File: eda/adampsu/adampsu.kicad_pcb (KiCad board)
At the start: 2 copper layers, 78.7 x 60.8 mm, 57 parts, among them J1 Barrel_Jack_Switch, J2 Conn_2Rows-09Pins, J3 DB9_Female, Q1 BUK7880-55A_CUX, SW1 30V 300mA Latching Switch, U1 TPS561201, U2 TPS54531DDAR

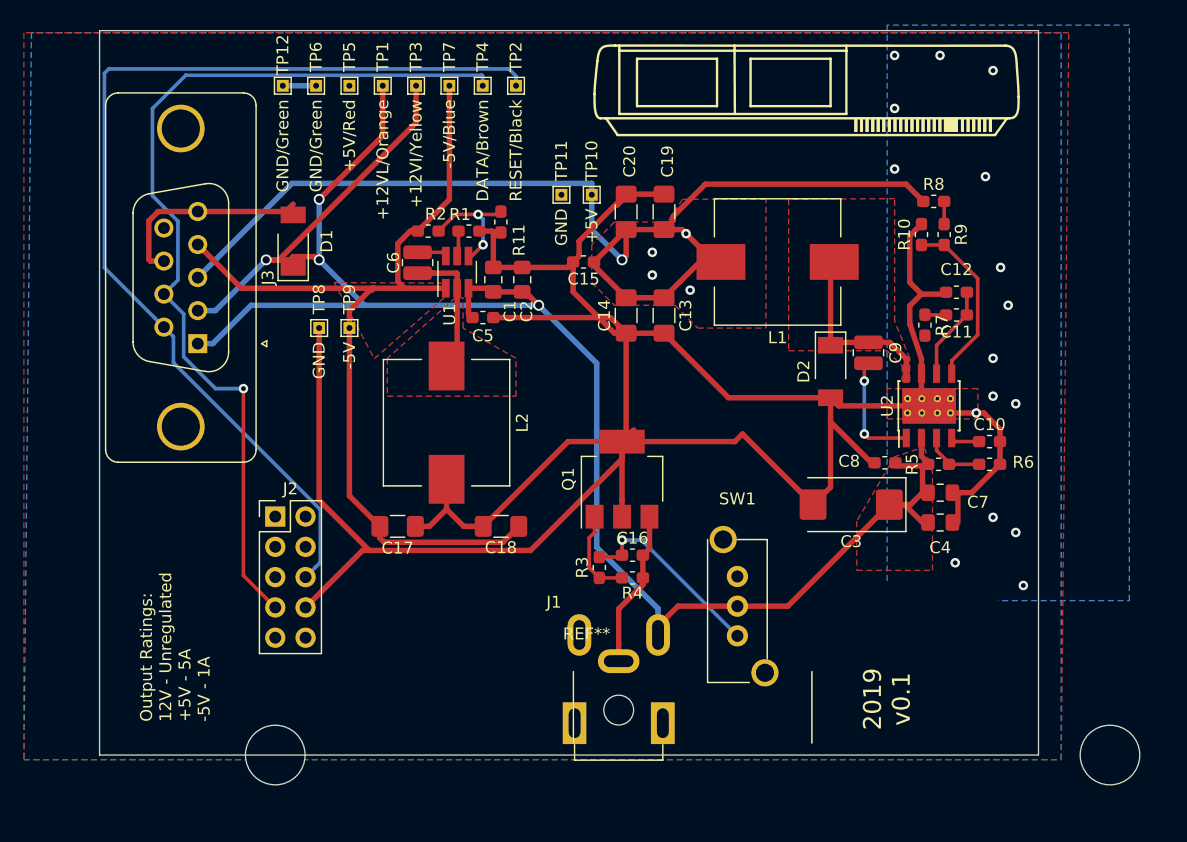
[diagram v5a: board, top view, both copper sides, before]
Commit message: high side switching
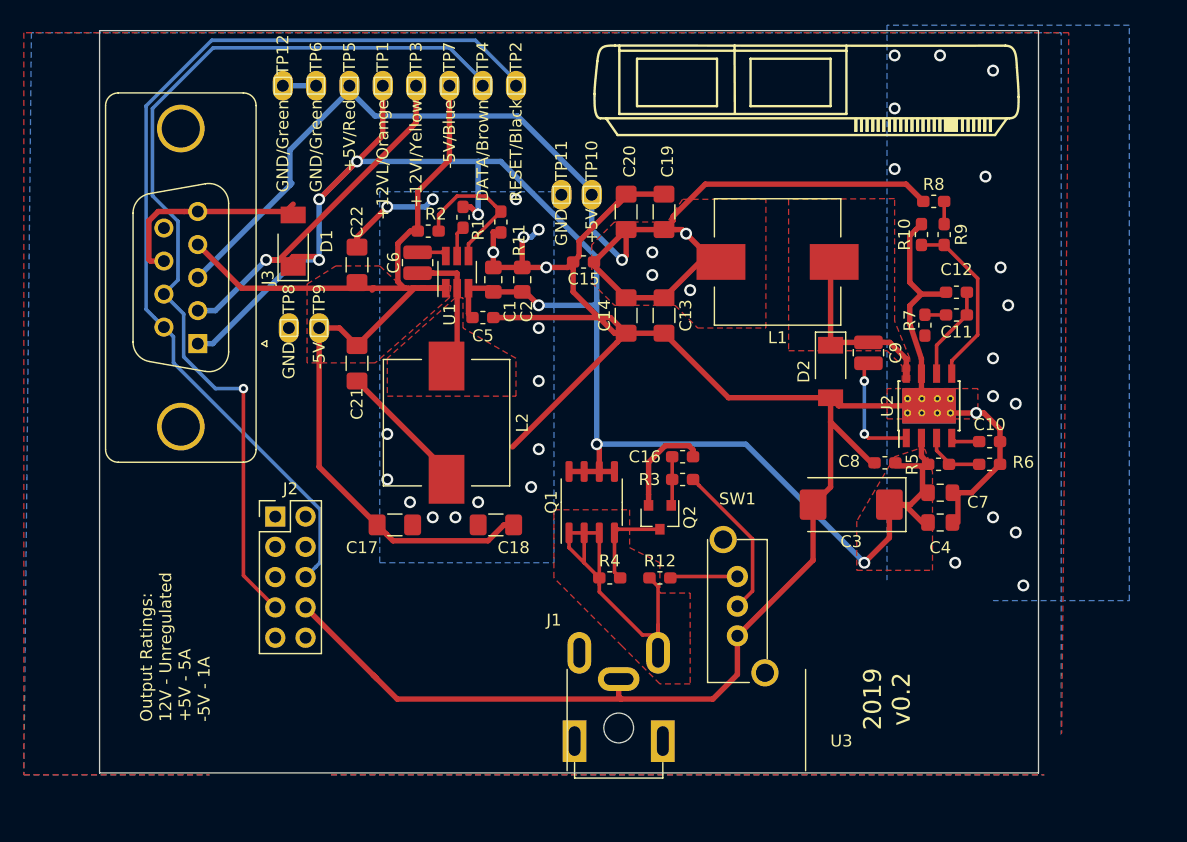
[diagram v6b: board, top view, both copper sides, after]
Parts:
- removed REF**: DB9-SpotMount, adampsu:DB9-SpotMount
- added C21: 22uF, Capacitor_SMD:C_1206_3216Metric_Pad1.42x1.75mm_HandSolder, F.Cu at (135.3, 85.5)
- added C22: 22uF, Capacitor_SMD:C_1206_3216Metric_Pad1.42x1.75mm_HandSolder, F.Cu at (135.3, 77.3)
- added Q2: Q_NPN_BEC, Package_TO_SOT_SMD:SOT-23, F.Cu at (160.7, 98.4)
- added R12: 100k, Resistor_SMD:R_0603_1608Metric_Pad1.05x0.95mm_HandSolder, F.Cu at (160.7, 103.5)
- added U3: Cuts, adampsu:DB9-SpotMount, F.Cu at (162.9, 118.2)
- Q1: value BUK7880-55A_CUX -> Si4447ADY; footprint Package_TO_SOT_SMD:SOT-223-3_TabPin2 -> Package_SO:SO-8_3.9x4.9mm_P1.27mm
- R4: value 10k -> 100k
- moved LB1 22.2 mm to (171.4, 67.9), turned to 180 degrees
- moved R3 10.2 mm to (162.6, 95.2), turned to 180 degrees
- moved C16 9.26 mm to (162.6, 93.3)
- moved Q1 3.19 mm to (154.9, 97.2)
- moved TP8 2.54 mm to (129.5, 82.5)
- moved TP9 2.54 mm to (132.1, 82.5)
- moved R4 1.91 mm to (156.4, 103.5)
- moved J1 1.50 mm to (157.2, 112.0)
- moved R1 1.26 mm to (144.1, 73.3), turned to 270 degrees
- moved C18 0.45 mm to (146.9, 99.1)
- moved C17 0.26 mm to (138.4, 99.1)
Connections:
- C16 pad 2: /GND-F -> GND
- J1 pad 1: +12V -> /12V-IN
- J1 pad 2: /GND-F -> GND
- Q1 pad 1: Net-(Q1-Pad1) -> /12V-IN
- Q1 pad 2: GND -> /12V-IN
- Q1 pad 3: /GND-F -> /12V-IN
- R1 pad 1: GND -> +12V
- R3 pad 1: Net-(Q1-Pad1) -> Net-(R3-Pad1)
- R4 pad 1: Net-(Q1-Pad1) -> /12V-IN
- R4 pad 2: /GND-F -> Net-(Q1-Pad4)
- SW1 pad 2: +12V -> Net-(R3-Pad1)
- SW1 pad 3: Net-(C16-Pad1) -> GND
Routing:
- net /12V-IN: track 0.00 -> 28.6 mm
- net +12V: track 164.4 -> 179.1 mm, vias 4 -> 8
- net Net-(R3-Pad1): track 0.00 -> 13.2 mm
- net /GND-F: track 13.2 -> 0.00 mm
- net Net-(C16-Pad1): track 16.4 -> 4.11 mm, vias 1 -> 0
- net +5V: track 96.8 -> 106.3 mm
- net /-5V: track 77.2 -> 86.4 mm
- net GND: track 253.2 -> 244.2 mm, vias 16 -> 33
- net Net-(Q1-Pad4): track 0.00 -> 7.91 mm
- net Net-(Q1-Pad1): track 7.58 -> 0.00 mm
- net Net-(R12-Pad2): track 0.00 -> 5.67 mm
- net /RESET: track 86.0 -> 82.0 mm
- net /DATA: track 78.1 -> 80.7 mm
- net Net-(R11-Pad2): track 10.2 -> 12.6 mm, vias 2 -> 0
- added copper zone on F.Cu, net /12V-IN
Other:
- board size 78.7 x 60.8 mm -> 78.7 x 62.2 mm
- net class Power: via_dia 0.9144 -> 1
- board text added: "2019 v0.2"
- board text removed: "2019 v0.1"

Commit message: This is dumb, don't use it. Rewiring top side switch
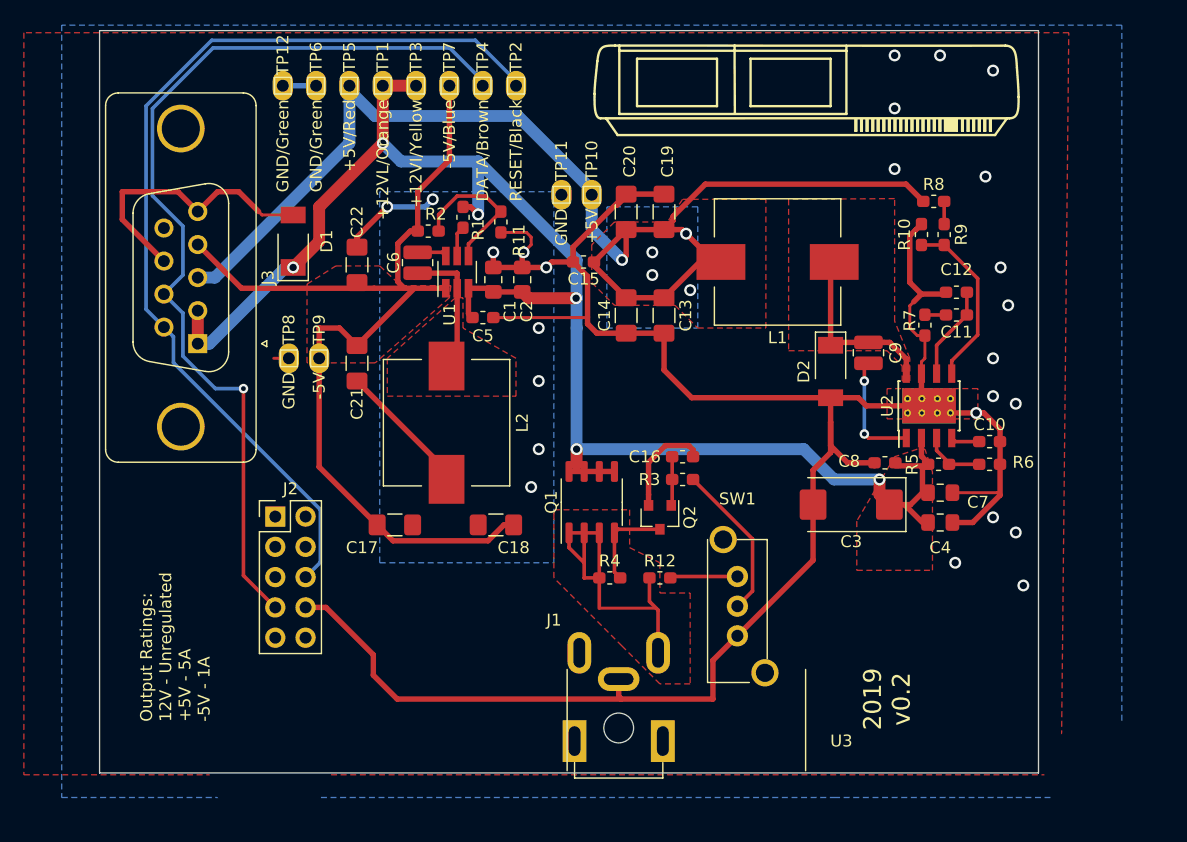
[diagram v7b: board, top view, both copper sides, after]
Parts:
- moved TP8 2.54 mm to (129.5, 85.1)
- moved TP9 2.54 mm to (132.1, 85.1)
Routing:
- net +12V: track 179.1 -> 135.8 mm, vias 8 -> 6
- net /-5V: track 86.4 -> 83.3 mm
- net GND: track 244.2 -> 243.2 mm, vias 33 -> 25
- net +5V: track 106.3 -> 105.3 mm
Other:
- net class Default removed
- net class Power removed

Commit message: Rerouted high side switch to be simpler and exported gerbers.
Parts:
- removed C16: 0.1uF, Capacitor_SMD:C_0603_1608Metric_Pad1.05x0.95mm_HandSolder
- removed Q2: Q_NPN_BEC, Package_TO_SOT_SMD:SOT-23
- removed R12: 100k, Resistor_SMD:R_0603_1608Metric_Pad1.05x0.95mm_HandSolder
- removed R3: 1k, Resistor_SMD:R_0603_1608Metric_Pad1.05x0.95mm_HandSolder
- added REFe: tt-logo, adampsu:tt-logo, B.Cu at (163.8, 87.6)
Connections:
- J1 pad 3: Net-(J1-Pad3) -> unconnected-(J1-Pad3)
- J2 pad 1: Net-(J2-Pad1) -> unconnected-(J2-Pad1)
- J2 pad 2: Net-(J2-Pad2) -> unconnected-(J2-Pad2)
- J2 pad 3: Net-(J2-Pad3) -> unconnected-(J2-Pad3)
- J2 pad 4: Net-(J2-Pad4) -> unconnected-(J2-Pad4)
- J2 pad 5: Net-(J2-Pad5) -> unconnected-(J2-Pad5)
- J2 pad 9: Net-(J2-Pad9) -> unconnected-(J2-Pad9)
- J3 pad 9: Net-(J3-Pad9) -> unconnected-(J3-Pad9)
- SW1 pad 1: Net-(R12-Pad2) -> GND
- SW1 pad 2: Net-(R3-Pad1) -> Net-(Q1-Pad4)
- SW1 pad 3: GND -> unconnected-(SW1-Pad3)
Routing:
- net Net-(R3-Pad1): track 13.2 -> 0.00 mm
- net Net-(Q1-Pad4): track 7.91 -> 15.2 mm
- net Net-(R12-Pad2): track 5.67 -> 0.00 mm
- net Net-(C16-Pad1): track 4.11 -> 0.00 mm
- net GND: track 243.2 -> 247.0 mm, vias 25 -> 24
- net /12V-IN: track 28.5 -> 25.5 mm
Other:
- board text added: "2023 v0.2.1"
- board text removed: "2019 v0.2"
